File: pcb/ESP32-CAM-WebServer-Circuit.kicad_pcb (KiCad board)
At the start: 2 copper layers, 30.5 x 48.3 mm, 12 parts, among them IC1 ESP32-CAM, J1 Conn_01x02, Q1 2N7002, Q2 IRLML0030, SW1 SW_SPDT, U1 TP4056-Module, U2 XC6503D331MR-G

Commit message: Update ESP32-CAM-WebServer-Circuit.kicad_pcb
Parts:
- moved SW1 4.84 mm to (163.4, 49.1)
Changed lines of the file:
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@@
   )
   (footprint "EG1270:EG1270" (layer "B.Cu")
-    (at 158.623 49.53 -90)
+    (at 163.449 49.149 -90)
     (descr "EG1270-1")
     (tags "Switch")
@@
   (segment (start 161.29 60.465) (end 159.7125 60.465) (width 0.4) (layer "F.Cu") (net 1))
   (segment (start 156.3425 57.748131) (end 157.964369 59.37) (width 0.4) (layer "F.Cu") (net 1))
-  (segment (start 153.623 49.53) (end 155.473 51.38) (width 0.25) (layer "F.Cu") (net 1))
+  (segment (start 158.449 49.149) (end 158.449 49.181) (width 0.25) (layer "F.Cu") (net 1))
   (segment (start 159.7125 60.465) (end 158.6175 59.37) (width 0.4) (layer "F.Cu") (net 1))
-  (segment (start 155.473 51.38) (end 156.25 51.38) (width 0.25) (layer "F.Cu") (net 1))
+  (segment (start 158.449 49.181) (end 156.25 51.38) (width 0.25) (layer "F.Cu") (net 1))
   (segment (start 156.3425 57.47) (end 156.3425 57.748131) (width 0.4) (layer "F.Cu") (net 1))
   (segment (start 160.02 60.96) (end 159.7125 60.6525) (width 0.4) (layer "F.Cu") (net 1))
@@
   (segment (start 156.03 65.86) (end 157.025 66.855) (width 0.4) (layer "F.Cu") (net 2))
   (segment (start 156.21 63.5) (end 156.21 63.005) (width 0.4) (layer "F.Cu") (net 2))
+  (segment (start 163.449 49.958) (end 161.25 52.157) (width 0.4) (layer "F.Cu") (net 2))
   (segment (start 172.3875 61.28) (end 172.8875 60.78) (width 0.25) (layer "F.Cu") (net 2))
   (segment (start 161.25 58.875) (end 161.29 58.915) (width 0.4) (layer "F.Cu") (net 2))
-  (segment (start 161.25 52.157) (end 161.25 58.875) (width 0.4) (layer "F.Cu") (net 2))
+  (segment (start 163.449 49.149) (end 163.449 49.958) (width 0.4) (layer "F.Cu") (net 2))
   (segment (start 161.25 58.875) (end 162.56 60.185) (width 0.4) (layer "F.Cu") (net 2))
   (segment (start 172.8875 60.78) (end 175.26 60.78) (width 0.25) (layer "F.Cu") (net 2))
@@
   (segment (start 153.85 65.86) (end 156.21 63.5) (width 0.4) (layer "F.Cu") (net 2))
   (segment (start 160.795 58.42) (end 158.6175 58.42) (width 0.4) (layer "F.Cu") (net 2))
+  (segment (start 161.25 52.157) (end 161.25 58.875) (width 0.4) (layer "F.Cu") (net 2))
   (segment (start 152.4 65.86) (end 156.03 65.86) (width 0.4) (layer "F.Cu") (net 2))
-  (segment (start 158.623 49.53) (end 161.25 52.157) (width 0.4) (layer "F.Cu") (net 2))
   (segment (start 156.3425 61.3225) (end 156.21 61.455) (width 0.4) (layer "F.Cu") (net 3))
   (segment (start 157.48 61.455) (end 156.21 61.455) (width 0.4) (layer "F.Cu") (net 3))
@@
   (segment (start 166.7025 56.83) (end 164.13067 59.40183) (width 1) (layer "F.Cu") (net 18))
   (segment (start 164.13067 65.17933) (end 160.025 69.285) (width 1) (layer "F.Cu") (net 18))
+  (segment (start 158.75 57.3375) (end 158.6175 57.47) (width 0.4) (layer "F.Cu") (net 22))
+  (segment (start 160.949 49.958) (end 158.75 52.157) (width 0.4) (layer "F.Cu") (net 22))
   (segment (start 158.75 52.157) (end 158.75 57.3375) (width 0.4) (layer "F.Cu") (net 22))
-  (segment (start 156.123 49.53) (end 158.75 52.157) (width 0.4) (layer "F.Cu") (net 22))
-  (segment (start 158.75 57.3375) (end 158.6175 57.47) (width 0.4) (layer "F.Cu") (net 22))
+  (segment (start 160.949 49.149) (end 160.949 49.958) (width 0.4) (layer "F.Cu") (net 22))
   (zone (net 21) (net_name "+5V") (layer "F.Cu") (name "+5V") (hatch edge 0.508)
     (priority 1)

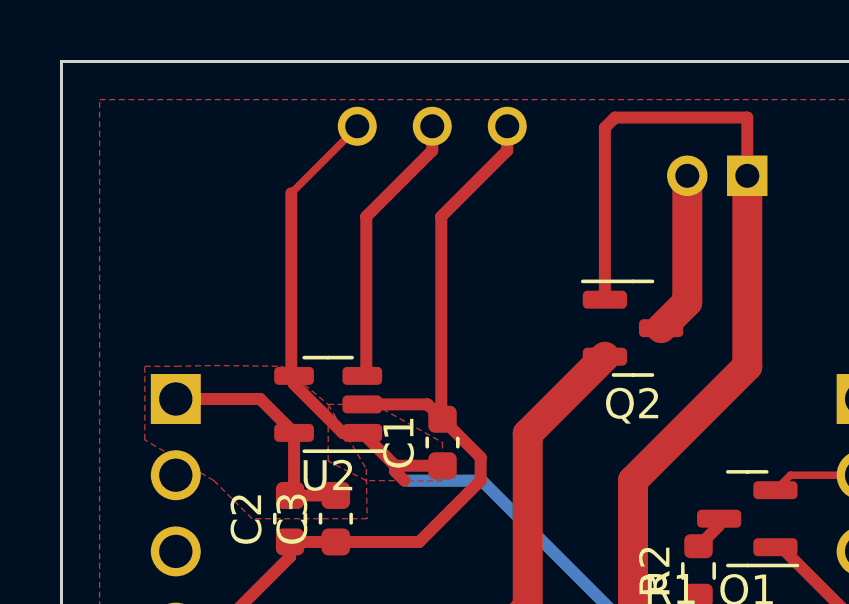
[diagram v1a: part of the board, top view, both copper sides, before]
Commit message: Revert all .kicad_pcb changes after 931255579d96a115043a583c4b53f5c496d14cc7
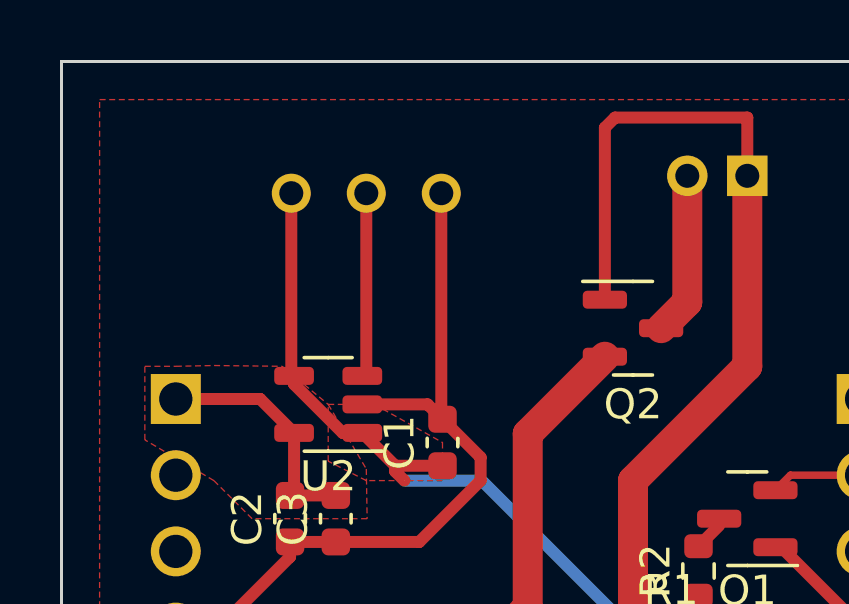
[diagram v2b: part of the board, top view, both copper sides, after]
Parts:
- moved SW1 3.13 mm to (161.2, 51.4)
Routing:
- net Net-(SW1-Pad2): track 9.29 -> 6.14 mm
- net Net-(C1-Pad1): track 30.6 -> 27.5 mm
- net GND: track 50.1 -> 46.9 mm
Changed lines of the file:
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@@
   )
   (footprint "EG1270:EG1270" (layer "B.Cu")
-    (at 163.449 49.149 -90)
+    (at 161.25 51.38 -90)
     (descr "EG1270-1")
     (tags "Switch")
@@
   (segment (start 161.29 60.465) (end 159.7125 60.465) (width 0.4) (layer "F.Cu") (net 1))
   (segment (start 156.3425 57.748131) (end 157.964369 59.37) (width 0.4) (layer "F.Cu") (net 1))
-  (segment (start 158.449 49.149) (end 158.449 49.181) (width 0.25) (layer "F.Cu") (net 1))
   (segment (start 159.7125 60.465) (end 158.6175 59.37) (width 0.4) (layer "F.Cu") (net 1))
-  (segment (start 158.449 49.181) (end 156.25 51.38) (width 0.25) (layer "F.Cu") (net 1))
   (segment (start 156.3425 57.47) (end 156.3425 57.748131) (width 0.4) (layer "F.Cu") (net 1))
   (segment (start 160.02 60.96) (end 159.7125 60.6525) (width 0.4) (layer "F.Cu") (net 1))
@@
   (segment (start 156.03 65.86) (end 157.025 66.855) (width 0.4) (layer "F.Cu") (net 2))
   (segment (start 156.21 63.5) (end 156.21 63.005) (width 0.4) (layer "F.Cu") (net 2))
-  (segment (start 163.449 49.958) (end 161.25 52.157) (width 0.4) (layer "F.Cu") (net 2))
   (segment (start 172.3875 61.28) (end 172.8875 60.78) (width 0.25) (layer "F.Cu") (net 2))
   (segment (start 161.25 58.875) (end 161.29 58.915) (width 0.4) (layer "F.Cu") (net 2))
-  (segment (start 163.449 49.149) (end 163.449 49.958) (width 0.4) (layer "F.Cu") (net 2))
   (segment (start 161.25 58.875) (end 162.56 60.185) (width 0.4) (layer "F.Cu") (net 2))
   (segment (start 172.8875 60.78) (end 175.26 60.78) (width 0.25) (layer "F.Cu") (net 2))
@@
   (segment (start 160.515 63.005) (end 157.48 63.005) (width 0.4) (layer "F.Cu") (net 2))
   (segment (start 162.56 60.96) (end 162.56 60.185) (width 0.4) (layer "F.Cu") (net 2))
+  (segment (start 161.25 51.38) (end 161.25 58.875) (width 0.4) (layer "F.Cu") (net 2))
   (segment (start 157.025 69.285) (end 157.025 75.129121) (width 0.4) (layer "F.Cu") (net 2))
   (segment (start 156.134121 76.02) (end 152.4 76.02) (width 0.4) (layer "F.Cu") (net 2))
   (segment (start 153.85 65.86) (end 156.21 63.5) (width 0.4) (layer "F.Cu") (net 2))
   (segment (start 160.795 58.42) (end 158.6175 58.42) (width 0.4) (layer "F.Cu") (net 2))
-  (segment (start 161.25 52.157) (end 161.25 58.875) (width 0.4) (layer "F.Cu") (net 2))
   (segment (start 152.4 65.86) (end 156.03 65.86) (width 0.4) (layer "F.Cu") (net 2))
   (segment (start 156.3425 61.3225) (end 156.21 61.455) (width 0.4) (layer "F.Cu") (net 3))
@@
   (segment (start 166.7025 56.83) (end 164.13067 59.40183) (width 1) (layer "F.Cu") (net 18))
   (segment (start 164.13067 65.17933) (end 160.025 69.285) (width 1) (layer "F.Cu") (net 18))
+  (segment (start 158.75 51.38) (end 158.75 57.3375) (width 0.4) (layer "F.Cu") (net 22))
   (segment (start 158.75 57.3375) (end 158.6175 57.47) (width 0.4) (layer "F.Cu") (net 22))
-  (segment (start 160.949 49.958) (end 158.75 52.157) (width 0.4) (layer "F.Cu") (net 22))
-  (segment (start 158.75 52.157) (end 158.75 57.3375) (width 0.4) (layer "F.Cu") (net 22))
-  (segment (start 160.949 49.149) (end 160.949 49.958) (width 0.4) (layer "F.Cu") (net 22))
   (zone (net 21) (net_name "+5V") (layer "F.Cu") (name "+5V") (hatch edge 0.508)
     (priority 1)

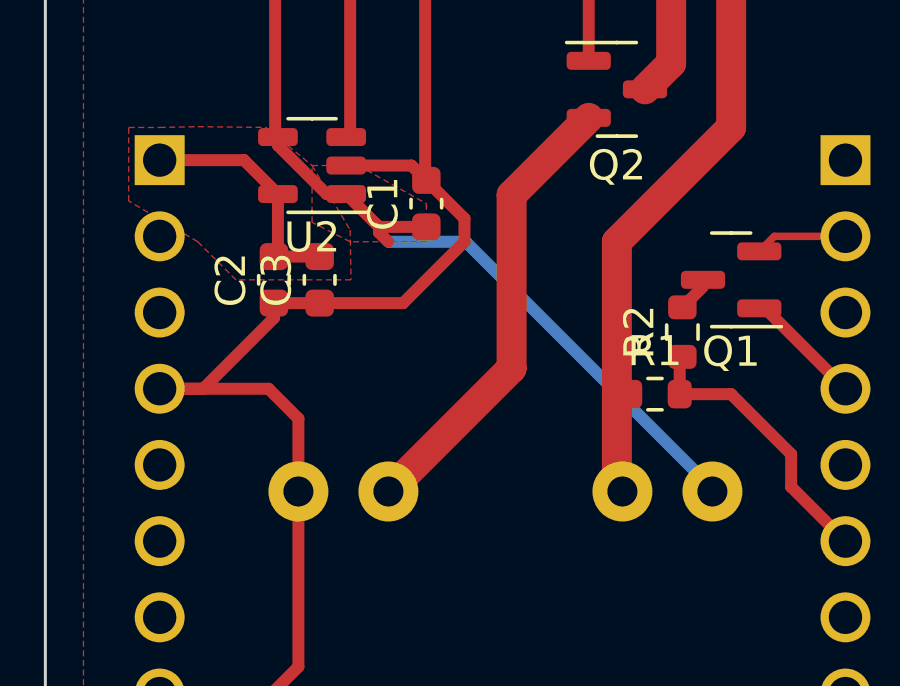
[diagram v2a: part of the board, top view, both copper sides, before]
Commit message: Move LiPo- Trace
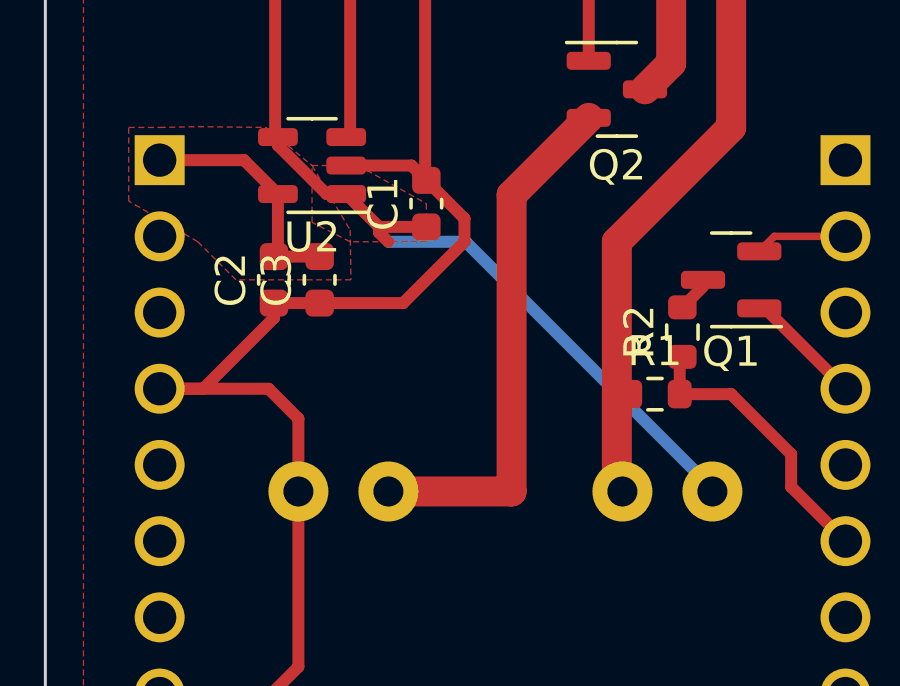
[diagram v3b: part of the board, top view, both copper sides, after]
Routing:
- net LiPo-: track 15.2 -> 17.6 mm
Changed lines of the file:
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@@
   (segment (start 169.45 50.8) (end 169.45 55.0075) (width 1) (layer "F.Cu") (net 17))
   (segment (start 169.45 55.0075) (end 168.5775 55.88) (width 1) (layer "F.Cu") (net 17))
-  (segment (start 164.13067 59.40183) (end 164.13067 65.17933) (width 1) (layer "F.Cu") (net 18))
+  (segment (start 164.13067 69.285) (end 160.025 69.285) (width 1) (layer "F.Cu") (net 18))
   (segment (start 166.7025 56.83) (end 164.13067 59.40183) (width 1) (layer "F.Cu") (net 18))
-  (segment (start 164.13067 65.17933) (end 160.025 69.285) (width 1) (layer "F.Cu") (net 18))
+  (segment (start 164.13067 59.40183) (end 164.13067 69.285) (width 1) (layer "F.Cu") (net 18))
   (segment (start 158.75 51.38) (end 158.75 57.3375) (width 0.4) (layer "F.Cu") (net 22))
   (segment (start 158.75 57.3375) (end 158.6175 57.47) (width 0.4) (layer "F.Cu") (net 22))
